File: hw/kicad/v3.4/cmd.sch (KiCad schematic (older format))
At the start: 17 parts

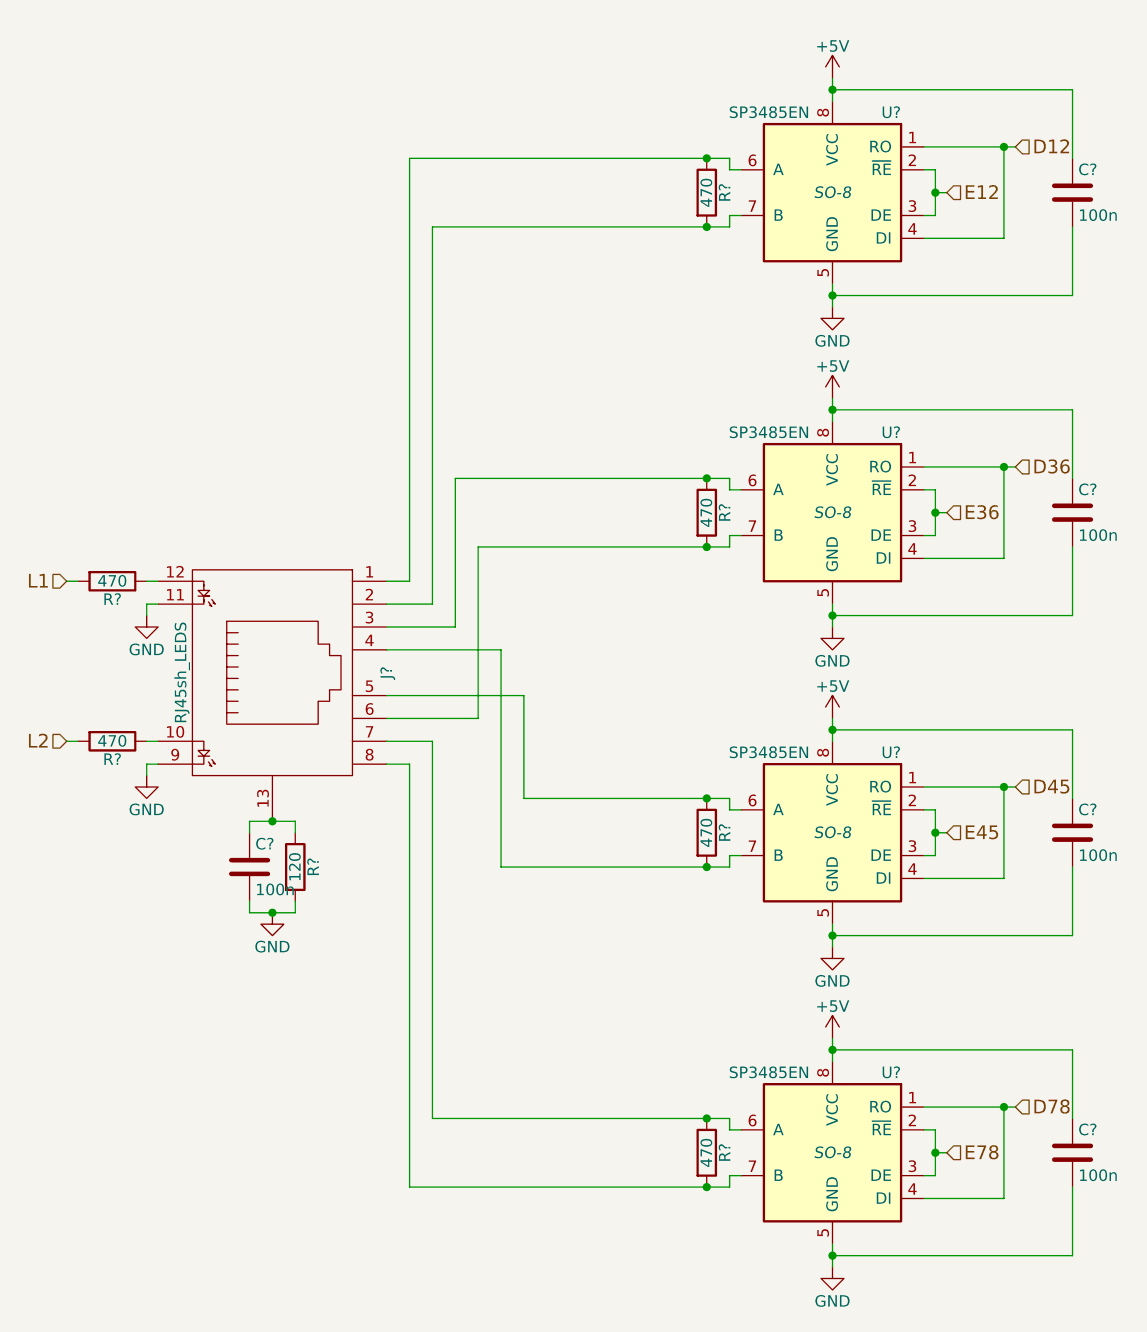
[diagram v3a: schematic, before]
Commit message: +f1 3.3V, viper fix
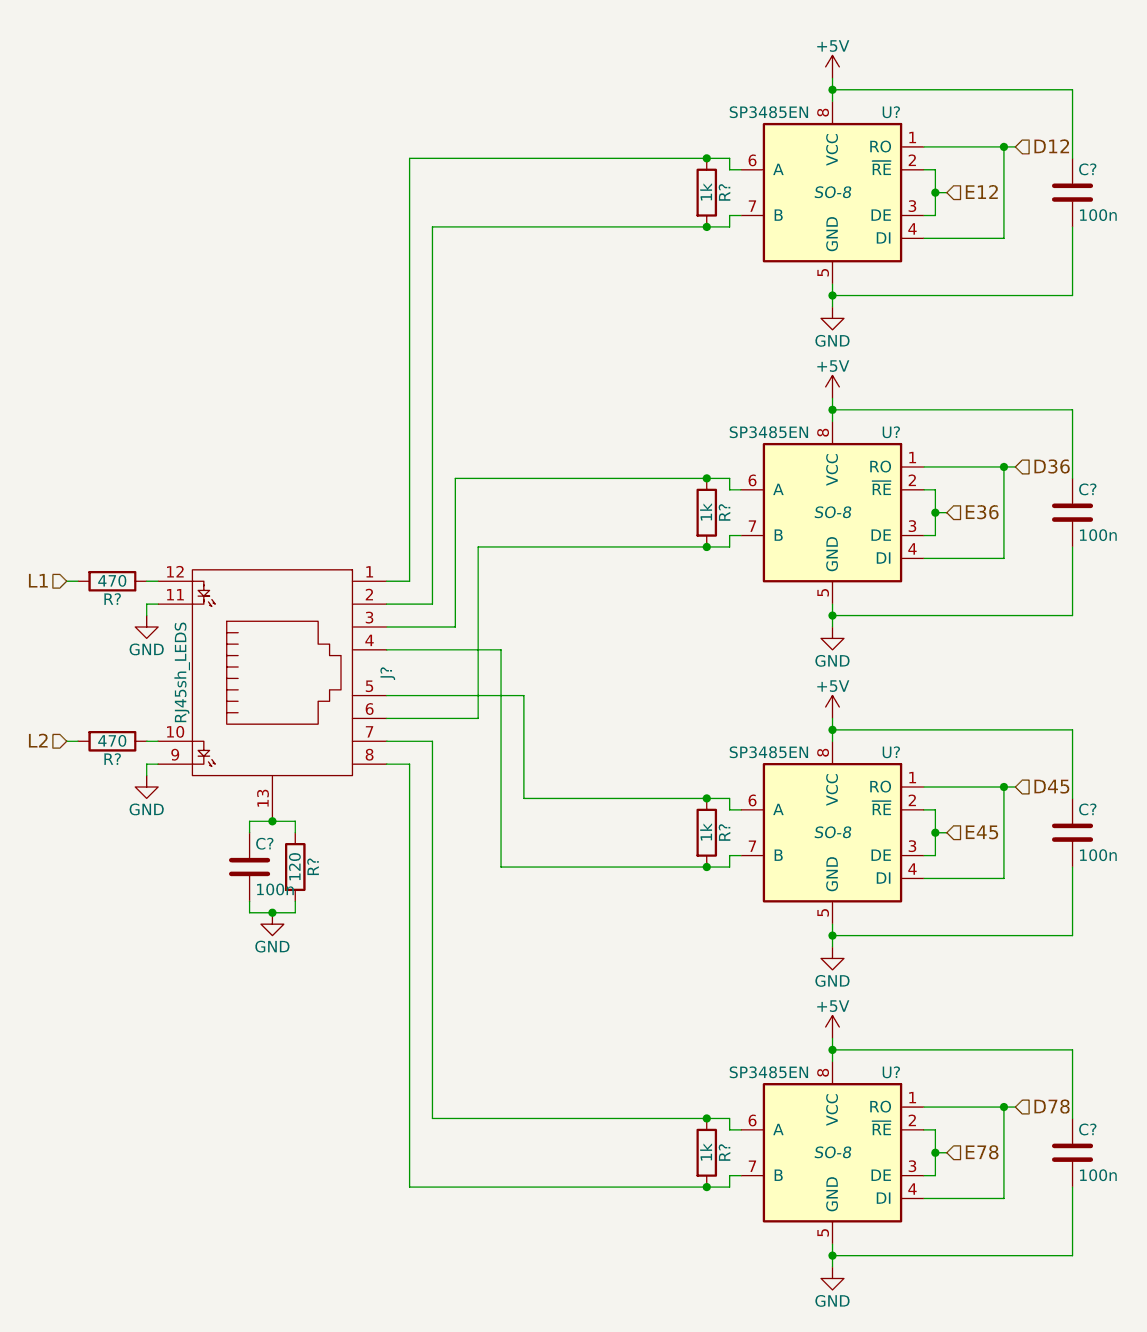
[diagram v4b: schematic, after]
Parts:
- R? (x4): value 470 -> 1k
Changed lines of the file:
@@
 $Descr A4 11693 8268
 encoding utf-8
-Sheet 9 15
+Sheet 10 15
 Title ""
 Date ""
@@
 P 4900 1400
 F 0 "R?" V 4980 1400 50  0000 C CNN
-F 1 "470" V 4900 1400 50  0000 C CNN
+F 1 "1k" V 4900 1400 50  0000 C CNN
 F 2 "" V 4830 1400 30  0000 C CNN
 F 3 "" H 4900 1400 30  0000 C CNN
@@
 P 4900 2800
 F 0 "R?" V 4980 2800 50  0000 C CNN
-F 1 "470" V 4900 2800 50  0000 C CNN
+F 1 "1k" V 4900 2800 50  0000 C CNN
 F 2 "" V 4830 2800 30  0000 C CNN
 F 3 "" H 4900 2800 30  0000 C CNN
@@
 P 4900 4200
 F 0 "R?" V 4980 4200 50  0000 C CNN
-F 1 "470" V 4900 4200 50  0000 C CNN
+F 1 "1k" V 4900 4200 50  0000 C CNN
 F 2 "" V 4830 4200 30  0000 C CNN
 F 3 "" H 4900 4200 30  0000 C CNN
@@
 P 4900 5600
 F 0 "R?" V 4980 5600 50  0000 C CNN
-F 1 "470" V 4900 5600 50  0000 C CNN
+F 1 "1k" V 4900 5600 50  0000 C CNN
 F 2 "" V 4830 5600 30  0000 C CNN
 F 3 "" H 4900 5600 30  0000 C CNN

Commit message: hw v3.4 +testpoints
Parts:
- added T? (x4): testpoint, symbol testpoint
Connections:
- net D12: now also T?.1
- net D36: now also T?.1
- net D45: now also T?.1
- net D78: now also T?.1
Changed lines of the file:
@@
 EESchema Schematic File Version 2
-LIBS:conn
 LIBS:power
 LIBS:stmbl_3.4-cache
@@
 Connection ~ 5900 1400
 Wire Wire Line
-	5850 1600 6200 1600
+	6200 1600 5850 1600
 Wire Wire Line
 	5850 2700 5900 2700
@@
 Connection ~ 5900 2800
 Wire Wire Line
-	5850 3000 6200 3000
+	6200 3000 5850 3000
 Wire Wire Line
 	5850 4100 5900 4100
@@
 Connection ~ 5900 4200
 Wire Wire Line
-	5850 4400 6200 4400
+	6200 4400 5850 4400
 Wire Wire Line
 	5850 5500 5900 5500
@@
 Connection ~ 5900 5600
 Wire Wire Line
-	5850 5800 6200 5800
+	6200 5800 5850 5800
 Wire Wire Line
 	3500 3100 3600 3100
@@
 Connection ~ 3000 4550
 Wire Wire Line
-	6200 1600 6200 1200
+	6200 1100 6200 1600
 Connection ~ 6200 1200
 Wire Wire Line
-	6200 3000 6200 2600
+	6200 2500 6200 3000
 Connection ~ 6200 2600
 Wire Wire Line
-	6200 5800 6200 5400
+	6200 5300 6200 5800
 Connection ~ 6200 5400
 Wire Wire Line
-	6200 4400 6200 4000
+	6200 3900 6200 4400
 Connection ~ 6200 4000
+$Comp
+L testpoint T?
+U 1 1 5681A9CE
+P 6200 5100
+F 0 "T?" H 6200 5200 60  0000 C CNN
+F 1 "testpoint" H 6200 5000 60  0000 C CNN
+F 2 "" H 6200 5100 60  0000 C CNN
+F 3 "" H 6200 5100 60  0000 C CNN
+	1    6200 5100
+	0    -1   -1   0
+$EndComp
+$Comp
+L testpoint T?
+U 1 1 5681AC45
+P 6200 3700
+F 0 "T?" H 6200 3800 60  0000 C CNN
+F 1 "testpoint" H 6200 3600 60  0000 C CNN
+F 2 "" H 6200 3700 60  0000 C CNN
+F 3 "" H 6200 3700 60  0000 C CNN
+	1    6200 3700
+	0    -1   -1   0
+$EndComp
+$Comp
+L testpoint T?
+U 1 1 5681AEA1
+P 6200 2300
+F 0 "T?" H 6200 2400 60  0000 C CNN
+F 1 "testpoint" H 6200 2200 60  0000 C CNN
+F 2 "" H 6200 2300 60  0000 C CNN
+F 3 "" H 6200 2300 60  0000 C CNN
+	1    6200 2300
+	0    -1   -1   0
+$EndComp
+$Comp
+L testpoint T?
+U 1 1 5681B104
+P 6200 900
+F 0 "T?" H 6200 1000 60  0000 C CNN
+F 1 "testpoint" H 6200 800 60  0000 C CNN
+F 2 "" H 6200 900 60  0000 C CNN
+F 3 "" H 6200 900 60  0000 C CNN
+	1    6200 900
+	0    -1   -1   0
+$EndComp
 $EndSCHEMATC

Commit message: v3.4
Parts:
- added JP? (x2): Jumper_NO_Small, symbol Jumper_NO_Small
- added R? (x8): 10k, symbol R
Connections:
- net +5V: now also JP?.1, R?.1, R?.1, R?.1, R?.1
- net GND: now also JP?.2, R?.2, R?.2, R?.2, R?.2
- net at J?.1, R?.1, U?.6 (A): now also R?.2
- net at J?.2, R?.2, U?.7 (B): now also R?.1
- net at J?.3, R?.1, U?.6 (A): now also R?.2
- net at J?.4, R?.2, U?.7 (B): now also R?.1
- net at J?.5, R?.1, U?.6 (A): now also R?.2
- net at J?.6, R?.2, U?.7 (B): now also R?.1
- net at J?.7, R?.1, U?.6 (A): now also JP?.2, R?.2
- net at J?.8, R?.2, U?.7 (B): now also JP?.1, R?.1
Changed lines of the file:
@@
 EESchema Schematic File Version 2
-LIBS:power
+LIBS:transistors
+LIBS:stm32
 LIBS:stmbl_3.4-cache
 EELAYER 25 0
@@
 $Descr A4 11693 8268
 encoding utf-8
-Sheet 10 15
+Sheet 10 14
 Title ""
 Date ""
@@
 	5000 1550 3700 1550
 Wire Wire Line
-	6500 1550 6500 1850
-Wire Wire Line
-	6500 1850 5450 1850
-Wire Wire Line
-	6500 1250 6500 950
-Wire Wire Line
-	6500 950  5450 950
+	6500 1850 6500 1550
+Wire Wire Line
+	5150 1850 6500 1850
+Wire Wire Line
+	6500 950  6500 1250
+Wire Wire Line
+	5150 950  6500 950
 Connection ~ 5450 950
 Connection ~ 5450 1850
@@
 	5000 2950 3900 2950
 Wire Wire Line
-	6500 2950 6500 3250
-Wire Wire Line
-	6500 3250 5450 3250
-Wire Wire Line
-	6500 2650 6500 2350
-Wire Wire Line
-	6500 2350 5450 2350
+	6500 3250 6500 2950
+Wire Wire Line
+	5150 3250 6500 3250
+Wire Wire Line
+	6500 2350 6500 2650
+Wire Wire Line
+	5150 2350 6500 2350
 Connection ~ 5450 2350
 Connection ~ 5450 3250
@@
 	5000 4350 4000 4350
 Wire Wire Line
-	6500 4350 6500 4650
-Wire Wire Line
-	6500 4650 5450 4650
-Wire Wire Line
-	6500 4050 6500 3750
-Wire Wire Line
-	6500 3750 5450 3750
+	6500 4650 6500 4350
+Wire Wire Line
+	5150 4650 6500 4650
+Wire Wire Line
+	6500 3750 6500 4050
+Wire Wire Line
+	5150 3750 6500 3750
 Connection ~ 5450 3750
 Connection ~ 5450 4650
@@
 	5000 5750 3600 5750
 Wire Wire Line
-	6500 5750 6500 6050
-Wire Wire Line
-	6500 6050 5450 6050
-Wire Wire Line
-	6500 5450 6500 5150
-Wire Wire Line
-	6500 5150 5450 5150
+	6500 6050 6500 5750
+Wire Wire Line
+	5150 6050 6500 6050
+Wire Wire Line
+	6500 5150 6500 5450
+Wire Wire Line
+	5150 5150 6500 5150
 Connection ~ 5450 5150
 Connection ~ 5450 6050
@@
 	0    -1   -1   0
 $EndComp
+$Comp
+L Jumper_NO_Small JP?
+U 1 1 56F9AAA1
+P 4650 5250
+F 0 "JP?" V 4650 5298 50  0000 L CNN
+F 1 "Jumper_NO_Small" H 4660 5190 50  0001 C CNN
+F 2 "" H 4650 5250 60  0000 C CNN
+F 3 "" H 4650 5250 60  0000 C CNN
+	1    4650 5250
+	0    1    1    0
+$EndComp
+$Comp
+L Jumper_NO_Small JP?
+U 1 1 56F9B07F
+P 4650 5950
+F 0 "JP?" V 4650 5998 50  0000 L CNN
+F 1 "Jumper_NO_Small" H 4660 5890 50  0001 C CNN
+F 2 "" H 4650 5950 60  0000 C CNN
+F 3 "" H 4650 5950 60  0000 C CNN
+	1    4650 5950
+	0    1    1    0
+$EndComp
+Wire Wire Line
+	4900 5350 4900 5450
+Wire Wire Line
+	4900 5850 4900 5750
+$Comp
+L R R?
+U 1 1 56F9D4F8
+P 4900 1000
+F 0 "R?" V 4980 1000 50  0000 C CNN
+F 1 "10k" V 4900 1000 50  0000 C CNN
+F 2 "" V 4830 1000 30  0000 C CNN
+F 3 "" H 4900 1000 30  0000 C CNN
+	1    4900 1000
+	1    0    0    -1
+$EndComp
+$Comp
+L R R?
+U 1 1 56F9D5CB
+P 4900 1800
+F 0 "R?" V 4980 1800 50  0000 C CNN
+F 1 "10k" V 4900 1800 50  0000 C CNN
+F 2 "" V 4830 1800 30  0000 C CNN
+F 3 "" H 4900 1800 30  0000 C CNN
+	1    4900 1800
+	1    0    0    -1
+$EndComp
+Wire Wire Line
+	4900 1650 4900 1550
+Wire Wire Line
+	4900 1250 4900 1150
+Wire Wire Line
+	4900 850  4900 750
+Wire Wire Line
+	4900 750  5150 750
+Wire Wire Line
+	5150 750  5150 950
+Wire Wire Line
+	4900 1950 4900 2050
+Wire Wire Line
+	4900 2050 5150 2050
+Wire Wire Line
+	5150 2050 5150 1850
+$Comp
+L R R?
+U 1 1 56F9E212
+P 4900 2400
+F 0 "R?" V 4980 2400 50  0000 C CNN
+F 1 "10k" V 4900 2400 50  0000 C CNN
+F 2 "" V 4830 2400 30  0000 C CNN
+F 3 "" H 4900 2400 30  0000 C CNN
+	1    4900 2400
+	1    0    0    -1
+$EndComp
+$Comp
+L R R?
+U 1 1 56F9E5E6
+P 4900 3200
+F 0 "R?" V 4980 3200 50  0000 C CNN
+F 1 "10k" V 4900 3200 50  0000 C CNN
+F 2 "" V 4830 3200 30  0000 C CNN
+F 3 "" H 4900 3200 30  0000 C CNN
+	1    4900 3200
+	1    0    0    -1
+$EndComp
+$Comp
+L R R?
+U 1 1 56F9EA0F
+P 4900 3800
+F 0 "R?" V 4980 3800 50  0000 C CNN
+F 1 "10k" V 4900 3800 50  0000 C CNN
+F 2 "" V 4830 3800 30  0000 C CNN
+F 3 "" H 4900 3800 30  0000 C CNN
+	1    4900 3800
+	1    0    0    -1
+$EndComp
+$Comp
+L R R?
+U 1 1 56F9EFAF
+P 4900 4600
+F 0 "R?" V 4980 4600 50  0000 C CNN
+F 1 "10k" V 4900 4600 50  0000 C CNN
+F 2 "" V 4830 4600 30  0000 C CNN
+F 3 "" H 4900 4600 30  0000 C CNN
+	1    4900 4600
+	1    0    0    -1
+$EndComp
+Wire Wire Line
+	4650 5350 4650 5450
+Connection ~ 4650 5450
+Wire Wire Line
+	4650 5850 4650 5750
+Connection ~ 4650 5750
+$Comp
+L R R?
+U 1 1 56F9FEE2
+P 4900 5200
+F 0 "R?" V 4980 5200 50  0000 C CNN
+F 1 "10k" V 4900 5200 50  0000 C CNN
+F 2 "" V 4830 5200 30  0000 C CNN
+F 3 "" H 4900 5200 30  0000 C CNN
+	1    4900 5200
+	1    0    0    -1
+$EndComp
+$Comp
+L R R?
+U 1 1 56F9FFE7
+P 4900 6000
+F 0 "R?" V 4980 6000 50  0000 C CNN
+F 1 "10k" V 4900 6000 50  0000 C CNN
+F 2 "" V 4830 6000 30  0000 C CNN
+F 3 "" H 4900 6000 30  0000 C CNN
+	1    4900 6000
+	1    0    0    -1
+$EndComp
+Wire Wire Line
+	4650 6050 4650 6250
+Wire Wire Line
+	4650 6250 5150 6250
+Wire Wire Line
+	5150 6250 5150 6050
+Wire Wire Line
+	4900 6150 4900 6250
+Connection ~ 4900 6250
+Wire Wire Line
+	4650 5150 4650 4950
+Wire Wire Line
+	4650 4950 5150 4950
+Wire Wire Line
+	5150 4950 5150 5150
+Wire Wire Line
+	4900 5050 4900 4950
+Connection ~ 4900 4950
+Wire Wire Line
+	4900 4750 4900 4850
+Wire Wire Line
+	4900 4850 5150 4850
+Wire Wire Line
+	5150 4850 5150 4650
+Wire Wire Line
+	4900 4450 4900 4350
+Wire Wire Line
+	4900 4050 4900 3950
+Wire Wire Line
+	4900 3650 4900 3550
+Wire Wire Line
+	4900 3550 5150 3550
+Wire Wire Line
+	5150 3550 5150 3750
+Wire Wire Line
+	4900 3050 4900 2950
+Wire Wire Line
+	4900 3350 4900 3450
+Wire Wire Line
+	4900 3450 5150 3450
+Wire Wire Line
+	5150 3450 5150 3250
+Wire Wire Line
+	4900 2650 4900 2550
+Wire Wire Line
+	4900 2250 4900 2150
+Wire Wire Line
+	4900 2150 5150 2150
+Wire Wire Line
+	5150 2150 5150 2350
 $EndSCHEMATC
